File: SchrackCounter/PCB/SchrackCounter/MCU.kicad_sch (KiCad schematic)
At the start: 3 parts, among them U6 ESP32-S3-WROOM-2

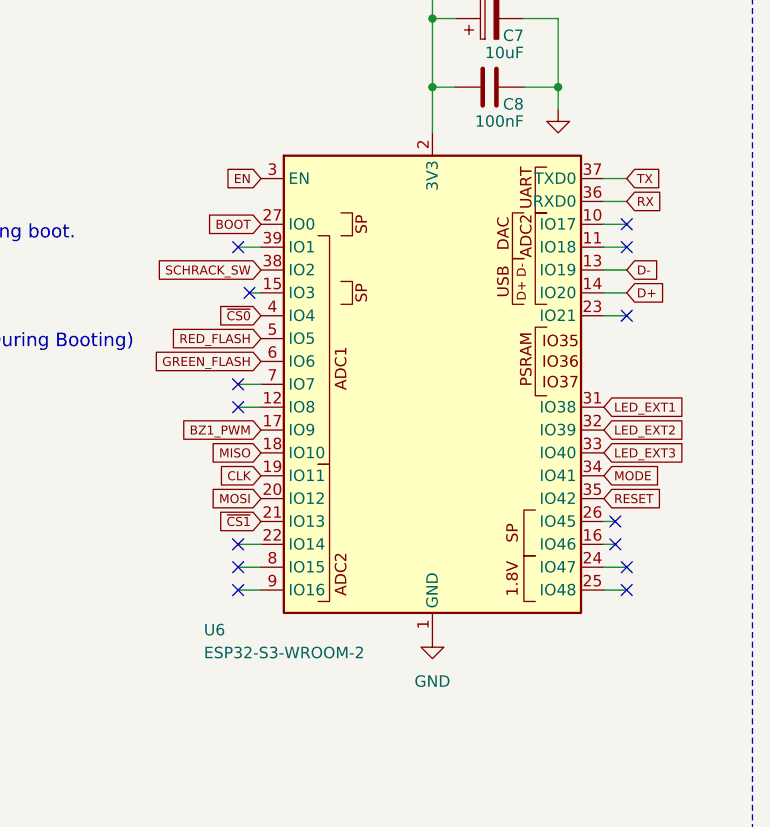
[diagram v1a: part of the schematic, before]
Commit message: Multiclock silkscreen updafe
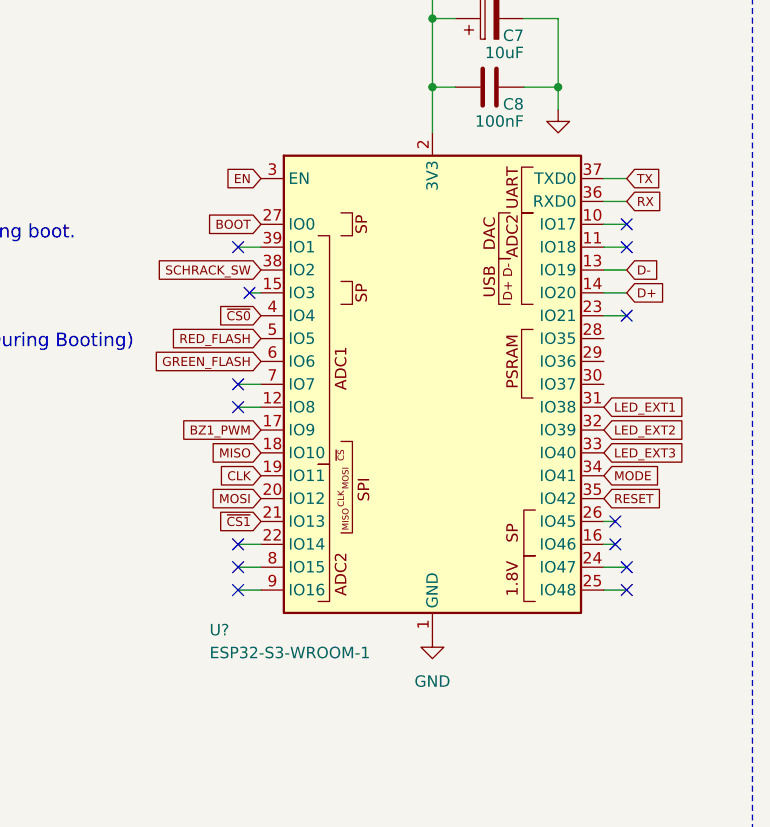
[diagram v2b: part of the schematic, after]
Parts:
- removed U6: ESP32-S3-WROOM-2, PCM_Espressif:ESP32-S3-WROOM-2, symbol sumec_sch_lib:ESP32-S3-WROOM-2_CUSTOM_made_by_bismarx
- added U?: ESP32-S3-WROOM-1, PCM_Espressif:ESP32-S3-WROOM-1, symbol sumec_sch_lib:ESP32-S3-WROOM-1_CUSTOM_made_by_bismarx
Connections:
- net +3V3: now also U?.2 (3V3)
- net BOOT: now also U?.27 (IO0)
- net BZ1_PWM: now also U?.17 (IO9)
- net CLK: now also U?.19 (IO11)
- net D+: now also U?.14 (IO20)
- net D-: now also U?.13 (IO19)
- net EN: now also U?.3 (EN)
- net GND: now also U?.1 (GND), U?.40 (GND), U?.41 (GND)
- net GREEN_FLASH: now also U?.6 (IO6)
- net LED_EXT1: now also U?.31 (IO38)
- net LED_EXT2: now also U?.32 (IO39)
- net LED_EXT3: now also U?.33 (IO40)
- net MISO: now also U?.18 (IO10)
- net MODE: now also U?.34 (IO41)
- net MOSI: now also U?.20 (IO12)
- net RED_FLASH: now also U?.5 (IO5)
- net RESET: now also U?.35 (IO42)
- net RX: now also U?.36 (RXD0)
- net SCHRACK_SW: now also U?.38 (IO2)
- net TX: now also U?.37 (TXD0)
- net ~{CS0}: now also U?.4 (IO4)
- net ~{CS1}: now also U?.21 (IO13)
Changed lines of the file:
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@@
-	)
-	(symbol
-		(lib_id "sumec_sch_lib:ESP32-S3-WROOM-2_CUSTOM_made_by_bismarx")
-		(at 201.93 96.52 0)
-		(unit 1)
-		(exclude_from_sim no)
-		(in_bom yes)
-		(on_board yes)
-		(dnp no)
-		(property "Reference" "U6"
-			(at 172.72 123.825 0)
-			(effects
-				(font
-					(size 1.27 1.27)
-				)
-				(justify left)
-			)
-		)
-		(property "Value" "ESP32-S3-WROOM-2"
-			(at 172.72 126.365 0)
-			(effects
-				(font
-					(size 1.27 1.27)
-				)
-				(justify left)
-			)
-		)
-		(property "Footprint" "PCM_Espressif:ESP32-S3-WROOM-2"
-			(at 199.136 53.086 0)
-			(effects
-				(font
-					(size 1.27 1.27)
-				)
-				(hide yes)
-			)
-		)
-		(property "Datasheet" "https://www.espressif.com/sites/default/files/documentation/esp32-s3-wroom-1_wroom-1u_datasheet_en.pdf"
-			(at 198.374 59.182 0)
-			(effects
-				(font
-					(size 1.27 1.27)
-				)
-				(hide yes)
-			)
-		)
-		(property "Description" "RF Module, ESP32-S3 SoC, Wi-Fi 802.11b/g/n, Bluetooth, BLE, 32-bit, 3.3V, onboard antenna, SMD"
-			(at 199.39 56.134 0)
-			(effects
-				(font
-					(size 1.27 1.27)
-				)
-				(hide yes)
-			)
-		)
-		(pin "40"
-		)
-		(pin "20"
-		)
-		(pin "27"
-		)
-		(pin "16"
-		)
-		(pin "23"
-		)
-		(pin "26"
-		)
-		(pin "12"
-		)
-		(pin "10"
-		)
-		(pin "4"
-		)
-		(pin "25"
-		)
-		(pin "41"
-		)
-		(pin "24"
-		)
-		(pin "19"
-		)
-		(pin "34"
-		)
-		(pin "33"
-		)
-		(pin "37"
-		)
-		(pin "38"
-		)
-		(pin "13"
-		)
-		(pin "14"
-		)
-		(pin "21"
-		)
-		(pin "32"
-		)
-		(pin "11"
-		)
-		(pin "22"
-		)
-		(pin "39"
-		)
-		(pin "7"
-		)
-		(pin "2"
-		)
-		(pin "6"
-		)
-		(pin "15"
-		)
-		(pin "31"
-		)
-		(pin "35"
-		)
-		(pin "36"
-		)
-		(pin "18"
-		)
-		(pin "1"
-		)
-		(pin "8"
-		)
-		(pin "9"
-		)
-		(pin "5"
-		)
-		(pin "3"
-		)
-		(pin "17"
-		)
-		(instances
-			(project "SchrackCounter"
-				(path "/d96f2ffc-3f4c-4f71-b693-29f6b8c3245d/39e148ed-9462-493d-862b-d9debebaa239"
-					(reference "U6")
-					(unit 1)
-				)
-			)
-		)
 	)
 	(symbol
@@
 					(unit 1)
 				)
+			)
+		)
+	)
+	(symbol
+		(lib_id "sumec_sch_lib:ESP32-S3-WROOM-1_CUSTOM_made_by_bismarx")
+		(at 201.93 96.52 0)
+		(unit 1)
+		(exclude_from_sim no)
+		(in_bom yes)
+		(on_board yes)
+		(dnp no)
+		(property "Reference" "U?"
+			(at 173.355 123.825 0)
+			(effects
+				(font
+					(size 1.27 1.27)
+				)
+				(justify left)
+			)
+		)
+		(property "Value" "ESP32-S3-WROOM-1"
+			(at 173.355 126.365 0)
+			(effects
+				(font
+					(size 1.27 1.27)
+				)
+				(justify left)
+			)
+		)
+		(property "Footprint" "PCM_Espressif:ESP32-S3-WROOM-1"
+			(at 199.136 53.086 0)
+			(effects
+				(font
+					(size 1.27 1.27)
+				)
+				(hide yes)
+			)
+		)
+		(property "Datasheet" "https://www.espressif.com/sites/default/files/documentation/esp32-s3-wroom-1_wroom-1u_datasheet_en.pdf"
+			(at 198.374 59.182 0)
+			(effects
+				(font
+					(size 1.27 1.27)
+				)
+				(hide yes)
+			)
+		)
+		(property "Description" "RF Module, ESP32-S3 SoC, Wi-Fi 802.11b/g/n, Bluetooth, BLE, 32-bit, 3.3V, onboard antenna, SMD"
+			(at 199.39 56.134 0)
+			(effects
+				(font
+					(size 1.27 1.27)
+				)
+				(hide yes)
+			)
+		)
+		(pin "17"
+		)
+		(pin "23"
+		)
+		(pin "16"
+		)
+		(pin "25"
+		)
+		(pin "29"
+		)
+		(pin "41"
+		)
+		(pin "26"
+		)
+		(pin "34"
+		)
+		(pin "39"
+		)
+		(pin "9"
+		)
+		(pin "19"
+		)
+		(pin "5"
+		)
+		(pin "31"
+		)
+		(pin "38"
+		)
+		(pin "1"
+		)
+		(pin "36"
+		)
+		(pin "20"
+		)
+		(pin "2"
+		)
+		(pin "14"
+		)
+		(pin "28"
+		)
+		(pin "37"
+		)
+		(pin "15"
+		)
+		(pin "21"
+		)
+		(pin "13"
+		)
+		(pin "12"
+		)
+		(pin "22"
+		)
+		(pin "24"
+		)
+		(pin "3"
+		)
+		(pin "4"
+		)
+		(pin "40"
+		)
+		(pin "11"
+		)
+		(pin "35"
+		)
+		(pin "30"
+		)
+		(pin "32"
+		)
+		(pin "7"
+		)
+		(pin "8"
+		)
+		(pin "33"
+		)
+		(pin "6"
+		)
+		(pin "18"
+		)
+		(pin "27"
+		)
+		(pin "10"
+		)
+		(instances
+			(project ""
+				(path "/d96f2ffc-3f4c-4f71-b693-29f6b8c3245d/39e148ed-9462-493d-862b-d9debebaa239"
+					(reference "U?")
+					(unit 1)
+				)

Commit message: PCB order plotting
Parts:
- gave numbers to parts that had none: 1
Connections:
- no-connect marks 14 -> 17
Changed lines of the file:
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@@
+	)
+	(no_connect
+		(at 219.71 93.98)
 	)
 	(no_connect
@@
 	)
 	(no_connect
+		(at 219.71 96.52)
+	)
+	(no_connect
 		(at 218.44 114.3)
 	)
 	(no_connect
-		(at 177.8 86.36)
+		(at 179.07 86.36)
 	)
 	(no_connect
@@
 	)
 	(no_connect
+		(at 219.71 91.44)
+	)
+	(no_connect
 		(at 176.53 99.06)
 	)
@@
 	(wire
 		(pts
+			(xy 217.17 91.44) (xy 219.71 91.44)
+		)
+		(stroke
+			(width 0)
+			(type default)
+		)
+	)
+	(wire
+		(pts
 			(xy 217.17 116.84) (xy 219.71 116.84)
 		)
@@
 	(wire
 		(pts
+			(xy 217.17 93.98) (xy 219.71 93.98)
+		)
+		(stroke
+			(width 0)
+			(type default)
+		)
+	)
+	(wire
+		(pts
 			(xy 217.17 78.74) (xy 219.71 78.74)
 		)
@@
 	(wire
 		(pts
+			(xy 217.17 96.52) (xy 219.71 96.52)
+		)
+		(stroke
+			(width 0)
+			(type default)
+		)
+	)
+	(wire
+		(pts
 			(xy 176.53 119.38) (xy 179.07 119.38)
 		)
@@
 		(pts
 			(xy 198.12 53.34) (xy 198.12 55.88)
-		)
-		(stroke
-			(width 0)
-			(type default)
-		)
-	)
-	(wire
-		(pts
-			(xy 177.8 86.36) (xy 179.07 86.36)
 		)
 		(stroke
@@
 		(on_board yes)
 		(dnp no)
-		(property "Reference" "#PWR012"
+		(property "Reference" "#PWR011"
 			(at 198.12 57.15 0)
 			(effects
@@
 			(project "SchrackCounter"
 				(path "/d96f2ffc-3f4c-4f71-b693-29f6b8c3245d/39e148ed-9462-493d-862b-d9debebaa239"
-					(reference "#PWR012")
+					(reference "#PWR011")
 					(unit 1)
 				)
@@
 		(dnp no)
 		(fields_autoplaced yes)
-		(property "Reference" "#PWR013"
+		(property "Reference" "#PWR012"
 			(at 198.12 130.81 0)
 			(effects
@@
 			(project "SchrackCounter"
 				(path "/d96f2ffc-3f4c-4f71-b693-29f6b8c3245d/39e148ed-9462-493d-862b-d9debebaa239"
-					(reference "#PWR013")
+					(reference "#PWR012")
 					(unit 1)
 				)
@@
 		(on_board yes)
 		(dnp no)
-		(property "Reference" "U?"
+		(property "Reference" "U6"
 			(at 173.355 123.825 0)
 			(effects
@@
 			(project ""
 				(path "/d96f2ffc-3f4c-4f71-b693-29f6b8c3245d/39e148ed-9462-493d-862b-d9debebaa239"
-					(reference "U?")
+					(reference "U6")
 					(unit 1)
 				)
@@
 		(dnp no)
 		(fields_autoplaced yes)
-		(property "Reference" "#PWR014"
+		(property "Reference" "#PWR013"
 			(at 212.09 72.39 0)
 			(effects
@@
 			(project "SchrackCounter"
 				(path "/d96f2ffc-3f4c-4f71-b693-29f6b8c3245d/39e148ed-9462-493d-862b-d9debebaa239"
-					(reference "#PWR014")
+					(reference "#PWR013")
 					(unit 1)
 				)
